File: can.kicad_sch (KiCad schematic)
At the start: 9 parts, among them U2 SN65HVD230

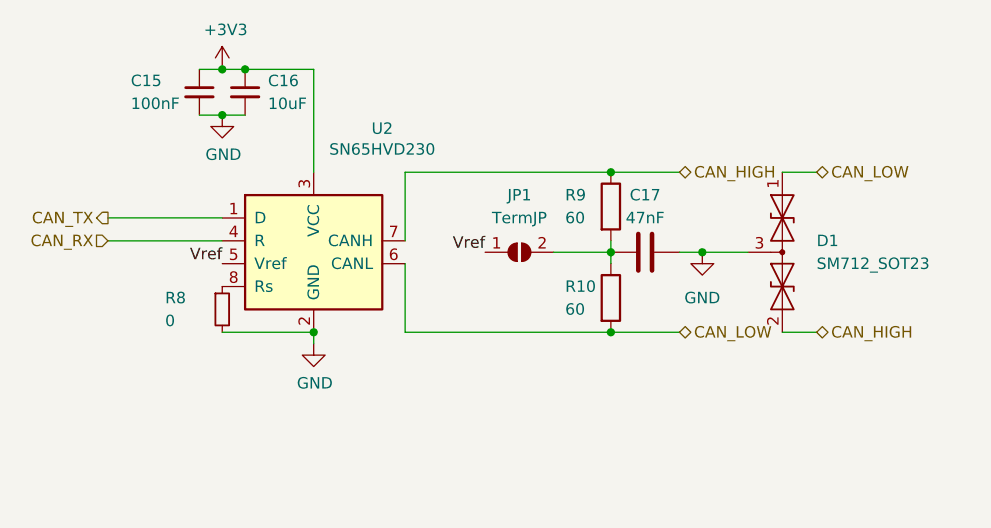
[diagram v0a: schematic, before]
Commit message: Fixed Libraries
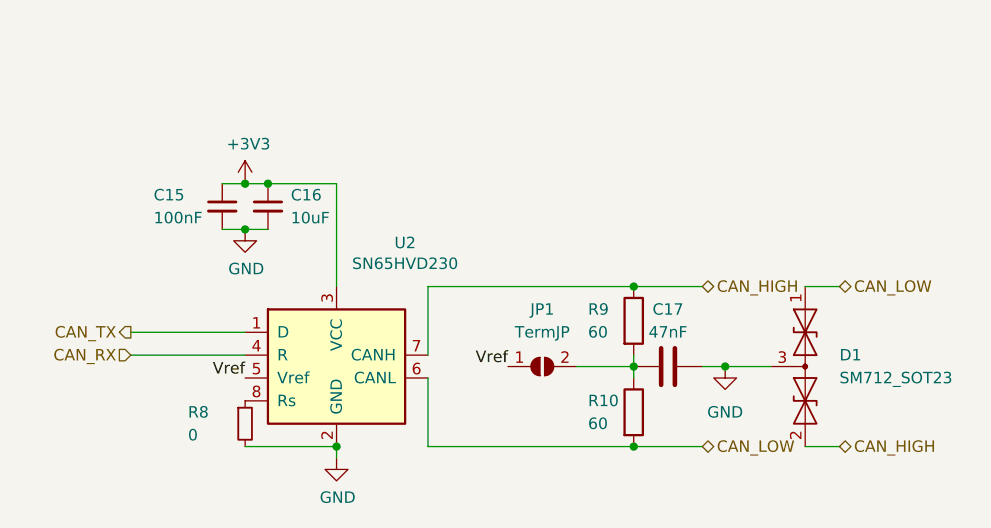
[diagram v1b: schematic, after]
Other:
- moved on the sheet: C15, C16, C17, D1, JP1, R10, R8, R9, U2

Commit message: Finishing touches without BOM
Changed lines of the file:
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@@
 (kicad_sch
-	(version 20231120)
+	(version 20250114)
 	(generator "eeschema")
-	(generator_version "8.0")
+	(generator_version "9.0")
 	(paper "A4")
 	(junction
@@
 	(label "Vref"
 		(at 127 102.87 180)
-		(fields_autoplaced yes)
 		(effects
 			(font
@@
 	(label "Vref"
 		(at 156.21 101.6 180)
-		(fields_autoplaced yes)
 		(effects
 			(font
@@
 		(shape input)
 		(at 114.3 100.33 180)
-		(fields_autoplaced yes)
 		(effects
 			(font
@@
 		(shape bidirectional)
 		(at 177.8 92.71 0)
-		(fields_autoplaced yes)
 		(effects
 			(font
@@
 		(shape output)
 		(at 114.3 97.79 180)
-		(fields_autoplaced yes)
 		(effects
 			(font
@@
 		(shape bidirectional)
 		(at 193.04 110.49 0)
-		(fields_autoplaced yes)
 		(effects
 			(font
@@
 		(shape bidirectional)
 		(at 193.04 92.71 0)
-		(fields_autoplaced yes)
 		(effects
 			(font
@@
 		(shape bidirectional)
 		(at 177.8 110.49 0)
-		(fields_autoplaced yes)
-		(effects
-			(font
+		(effects
+			(font
